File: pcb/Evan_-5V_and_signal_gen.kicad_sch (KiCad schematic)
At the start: 36 parts, among them IC1 TL7660IDGKR, IC2 TL081IDT, U2 LTC4300A-1IMS8_PBF, U4 TPS79933QDDCRQ1, U5 TPS2069CDBVR_MOSFET

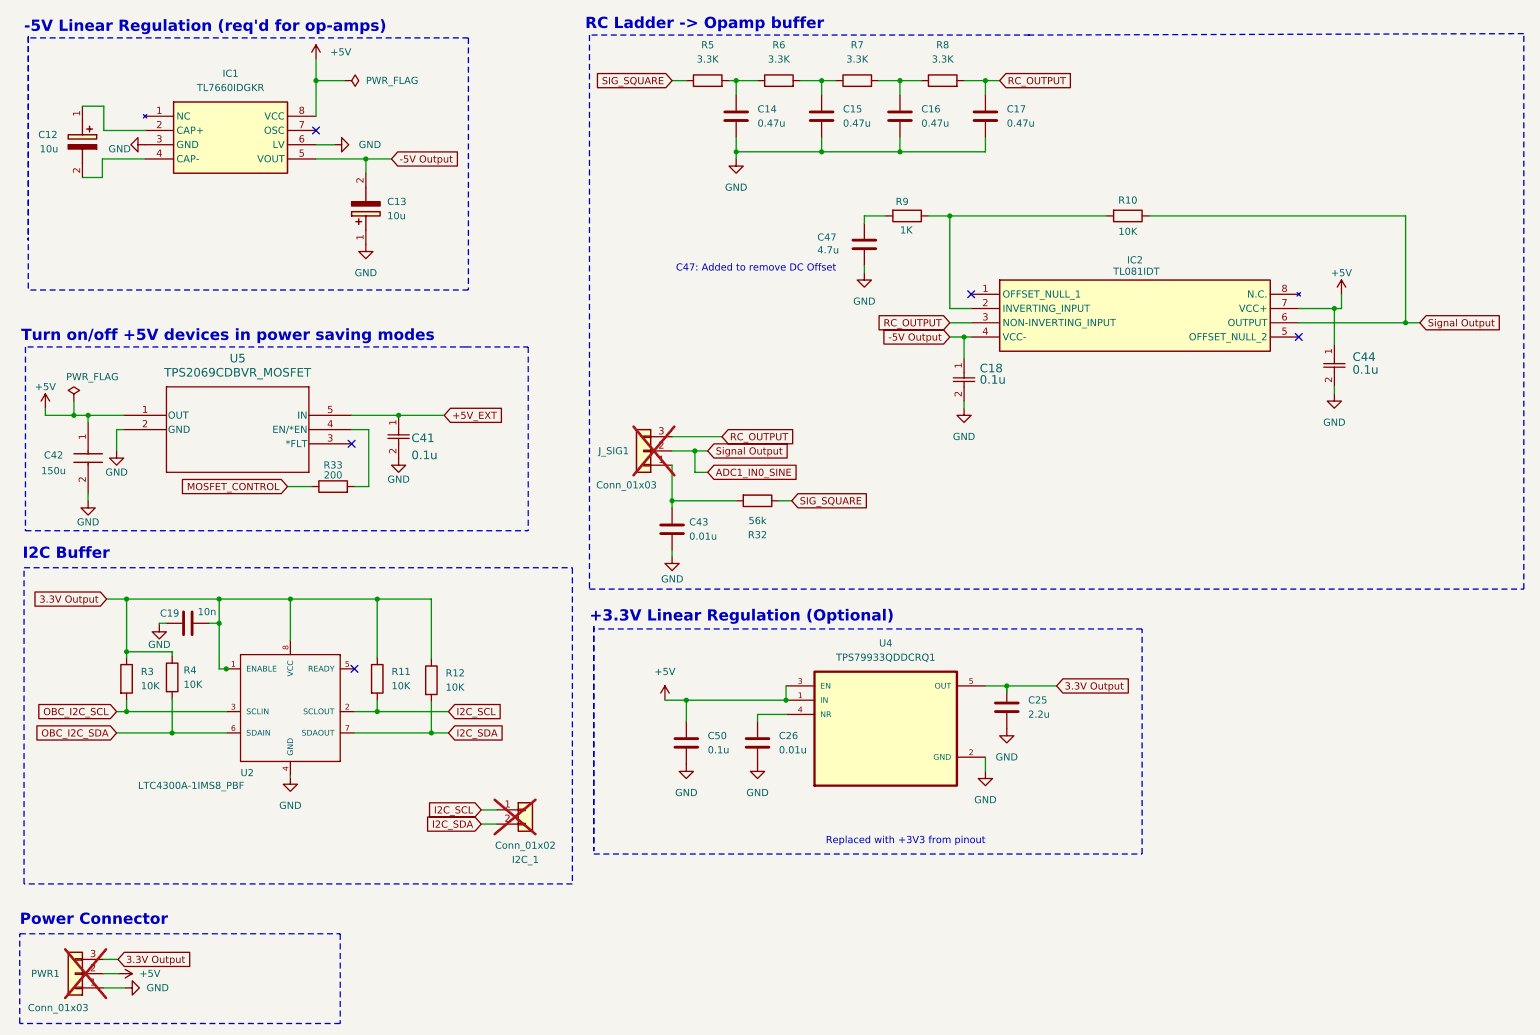
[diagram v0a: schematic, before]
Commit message: Replaced wire to board connectors with screw terminals
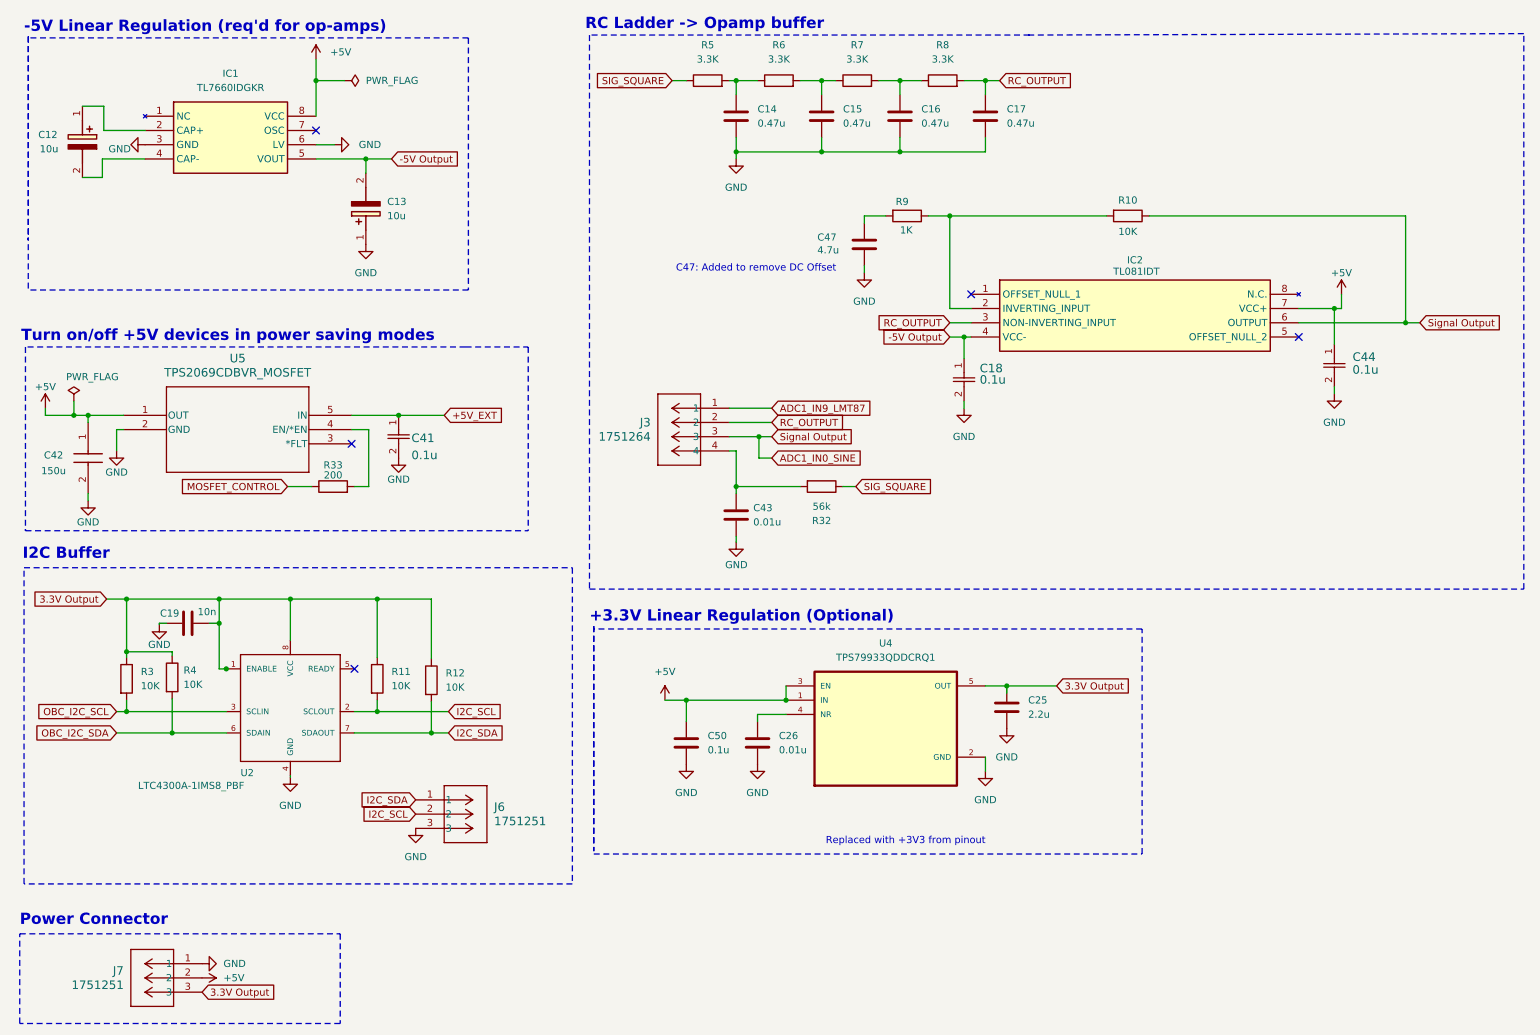
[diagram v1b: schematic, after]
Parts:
- removed I2C_1: Conn_01x02, Connector_PinHeader_2.54mm:PinHeader_1x02_P2.54mm_Vertical, symbol Connector_Generic:Conn_01x02
- removed J_SIG1, PWR1: Conn_01x03, Connector_PinHeader_2.54mm:PinHeader_1x03_P2.54mm_Vertical, symbol Connector_Generic:Conn_01x03
- added J3: 1751264, Screw Terminal 1x4:CONN_1751264_PXC, symbol Screw Terminal 1x4:1751264
- added J6, J7: 1751251, Screw Terminal 1x3:CONN_1751251_PXC, symbol Screw Terminal 1x3:1751251
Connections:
- net +5V: now also J7.2
- net 3.3V Output: now also J7.3
- net ADC1_IN0_SINE: now also J3.3
- net GND: now also J6.3, J7.1
- net I2C_SCL: now also J6.2
- net I2C_SDA: now also J6.1
- net RC_OUTPUT: now also J3.2
- net at C43.2, R32.2: now also J3.4
- new net ADC1_IN9_LMT87: J3.1
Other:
- moved on the sheet: C43, R32
